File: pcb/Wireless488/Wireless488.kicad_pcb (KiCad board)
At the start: 2 copper layers, 74 x 60 mm, 7 parts, among them J1 Centronics 24 Pin, J2 Power, U1 ESP32_DevKitC

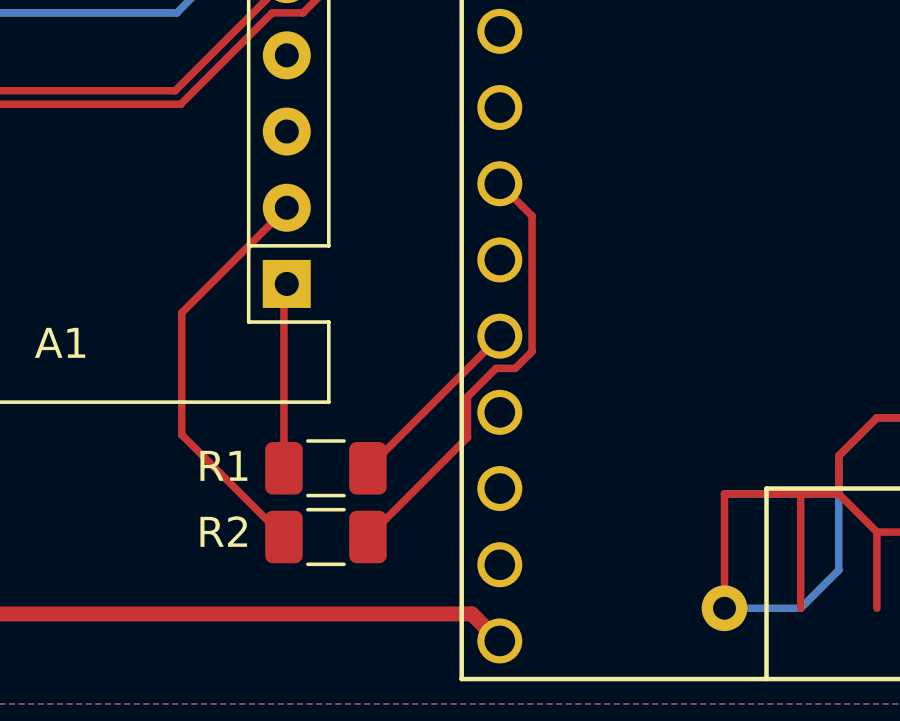
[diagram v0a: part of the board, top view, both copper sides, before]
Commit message: PCB Tidy, improved examples for laser monitoring
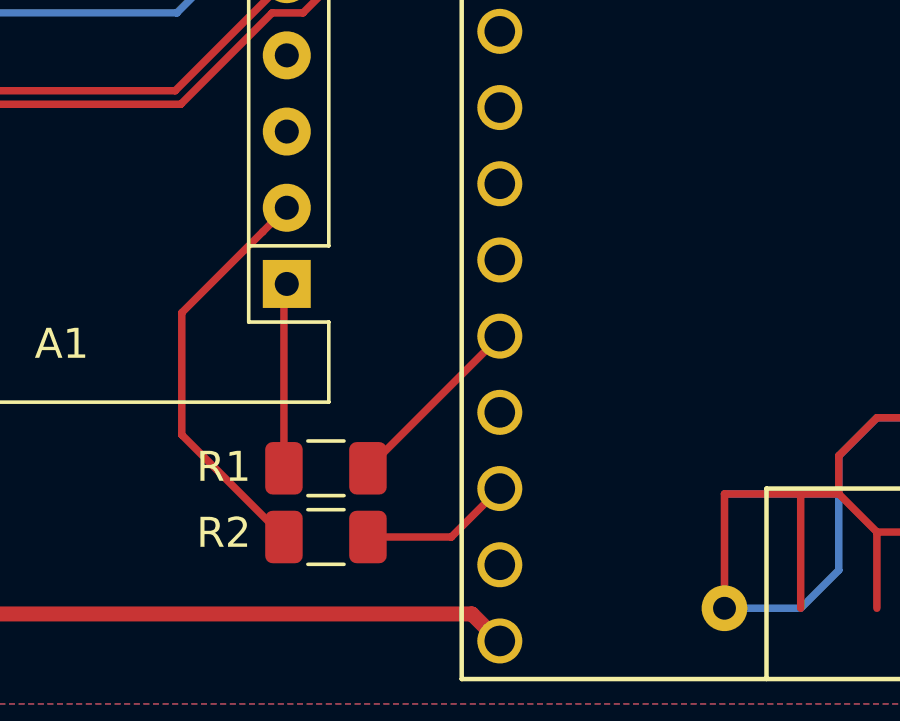
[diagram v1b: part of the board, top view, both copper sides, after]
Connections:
- R2 pad 2: Net-(R2-Pad2) -> /ESP_TX
- U1 pad 13: Net-(R2-Pad2) -> Net-(U1-Pad13)
- U1 pad 17: Net-(U1-Pad17) -> /ESP_TX
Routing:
- net Net-(R2-Pad2): track 14.9 -> 0.00 mm
- net /ESP_TX: track 0.00 -> 5.06 mm
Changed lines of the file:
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@@
-(kicad_pcb (version 20171130) (host pcbnew 5.0.2+dfsg1-1)
+(kicad_pcb (version 20171130) (host pcbnew 5.0.2-bee76a0~70~ubuntu18.04.1)
   (general
     (thickness 1.6)
     (drawings 9)
-    (tracks 133)
+    (tracks 127)
     (zones 0)
     (modules 7)
@@
   (net 60 "Net-(U1-Pad37)")
   (net 61 "Net-(R1-Pad2)")
-  (net 62 "Net-(R2-Pad2)")
-  (net 63 "Net-(U1-Pad17)")
-  (net 64 "Net-(U1-Pad16)")
+  (net 62 "Net-(U1-Pad16)")
+  (net 63 /ESP_TX)
+  (net 64 "Net-(U1-Pad13)")
   (net_class Default "This is the default net class."
     (clearance 0.2)
@@
     (add_net /DIO8)
     (add_net /EOI)
+    (add_net /ESP_TX)
     (add_net /IFC)
     (add_net /NDAC)
@@
     (add_net "Net-(A1-Pad9)")
     (add_net "Net-(R1-Pad2)")
-    (add_net "Net-(R2-Pad2)")
     (add_net "Net-(U1-Pad1)")
     (add_net "Net-(U1-Pad10)")
     (add_net "Net-(U1-Pad11)")
     (add_net "Net-(U1-Pad12)")
+    (add_net "Net-(U1-Pad13)")
     (add_net "Net-(U1-Pad16)")
-    (add_net "Net-(U1-Pad17)")
     (add_net "Net-(U1-Pad18)")
     (add_net "Net-(U1-Pad2)")
@@
       (net 43 "Net-(U1-Pad18)"))
     (pad 17 thru_hole circle (at -12.7 20.32) (size 1.5 1.5) (drill 1.02) (layers *.Cu *.Mask)
-      (net 63 "Net-(U1-Pad17)"))
+      (net 63 /ESP_TX))
     (pad 16 thru_hole circle (at -12.7 17.78) (size 1.5 1.5) (drill 1.02) (layers *.Cu *.Mask)
-      (net 64 "Net-(U1-Pad16)"))
+      (net 62 "Net-(U1-Pad16)"))
     (pad 15 thru_hole circle (at -12.7 15.24) (size 1.5 1.5) (drill 1.02) (layers *.Cu *.Mask)
       (net 61 "Net-(R1-Pad2)"))
@@
       (net 7 GND))
     (pad 13 thru_hole circle (at -12.7 10.16) (size 1.5 1.5) (drill 1.02) (layers *.Cu *.Mask)
-      (net 62 "Net-(R2-Pad2)"))
+      (net 64 "Net-(U1-Pad13)"))
     (pad 12 thru_hole circle (at -12.7 7.62) (size 1.5 1.5) (drill 1.02) (layers *.Cu *.Mask)
       (net 42 "Net-(U1-Pad12)"))
@@
     (fp_line (start -1.6 0.8) (end -1.6 -0.8) (layer F.Fab) (width 0.1))
     (pad 2 smd roundrect (at 1.4 0) (size 1.25 1.75) (layers F.Cu F.Paste F.Mask) (roundrect_rratio 0.2)
-      (net 62 "Net-(R2-Pad2)"))
+      (net 63 /ESP_TX))
     (pad 1 smd roundrect (at -1.4 0) (size 1.25 1.75) (layers F.Cu F.Paste F.Mask) (roundrect_rratio 0.2)
       (net 3 "Net-(A1-Pad2)"))
@@
   (segment (start 134.1 96.750002) (end 134.1 96.74) (width 0.25) (layer F.Cu) (net 61))
   (segment (start 129.705001 101.145001) (end 134.1 96.750002) (width 0.25) (layer F.Cu) (net 61))
-  (segment (start 135.175001 97.256001) (end 135.175001 92.735001) (width 0.25) (layer F.Cu) (net 62))
-  (segment (start 135.175001 92.735001) (end 134.849999 92.409999) (width 0.25) (layer F.Cu) (net 62))
-  (segment (start 134.616001 97.815001) (end 135.175001 97.256001) (width 0.25) (layer F.Cu) (net 62))
-  (segment (start 133.973997 97.815001) (end 134.616001 97.815001) (width 0.25) (layer F.Cu) (net 62))
-  (segment (start 133.024999 98.763999) (end 133.973997 97.815001) (width 0.25) (layer F.Cu) (net 62))
-  (segment (start 133.024999 100.115003) (end 133.024999 98.763999) (width 0.25) (layer F.Cu) (net 62))
-  (segment (start 134.849999 92.409999) (end 134.1 91.66) (width 0.25) (layer F.Cu) (net 62))
-  (segment (start 129.705001 103.435001) (end 133.024999 100.115003) (width 0.25) (layer F.Cu) (net 62))
+  (segment (start 132.484999 103.435001) (end 134.1 101.82) (width 0.25) (layer F.Cu) (net 63))
+  (segment (start 129.705001 103.435001) (end 132.484999 103.435001) (width 0.25) (layer F.Cu) (net 63))
   (zone (net 0) (net_name "") (layers F&B.Cu) (hatch edge 0.508)
     (connect_pads (clearance 0.508))
